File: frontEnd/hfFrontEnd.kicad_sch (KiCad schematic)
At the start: 14 parts

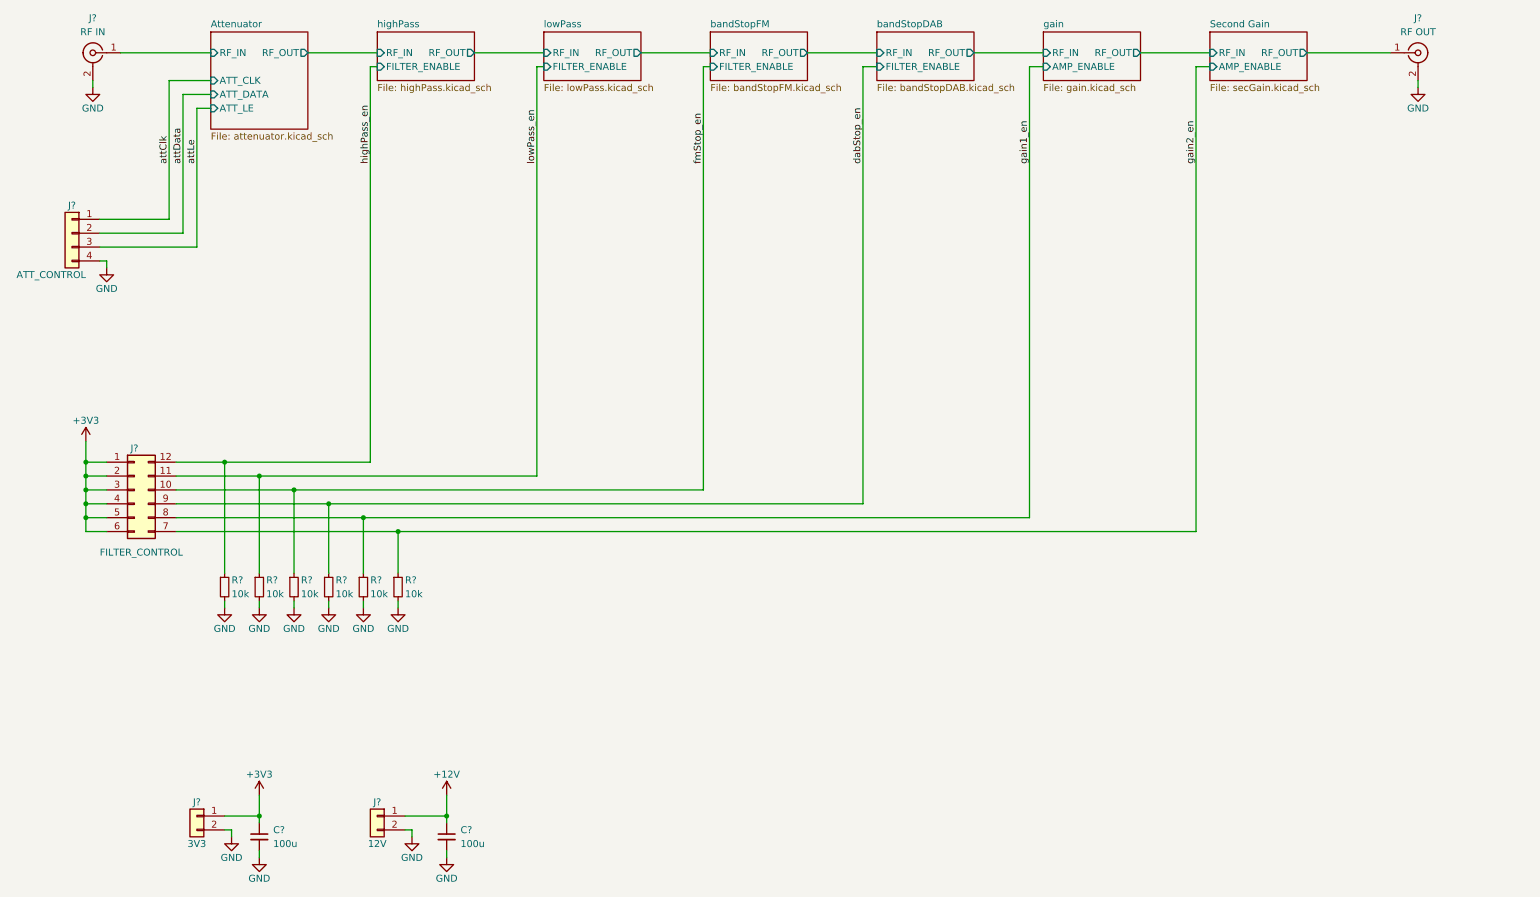
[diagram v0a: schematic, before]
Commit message: update schematics, add bypass for the attenuator
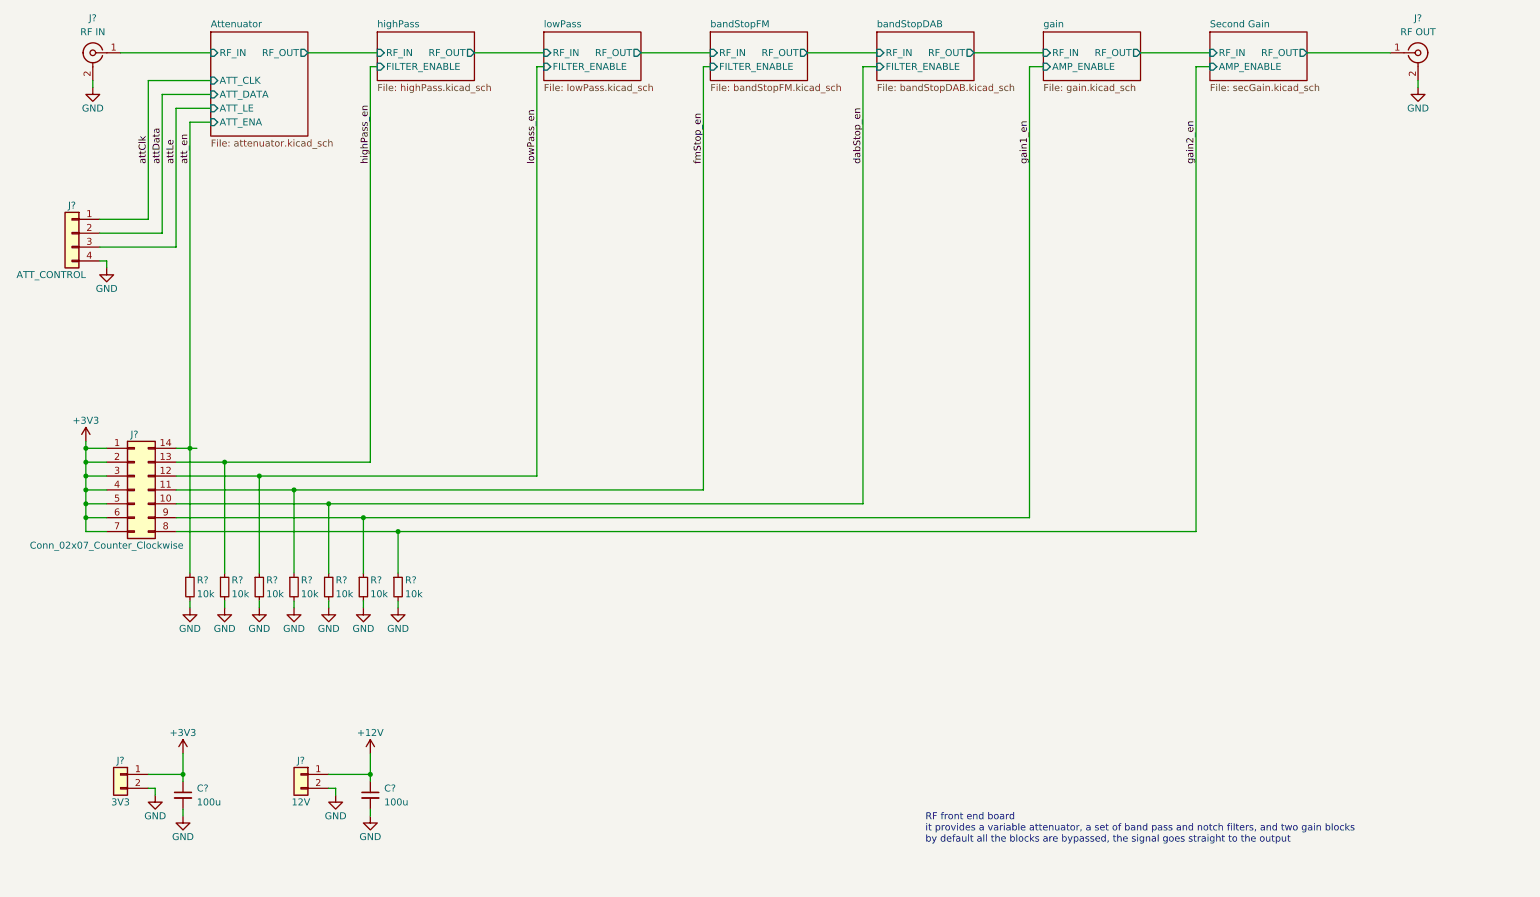
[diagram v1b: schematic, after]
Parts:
- removed J?: FILTER_CONTROL, symbol Connector_Generic:Conn_02x06_Counter_Clockwise
- added J?: Conn_02x07_Counter_Clockwise, symbol Connector_Generic:Conn_02x07_Counter_Clockwise
- added R?: 10k, symbol Device:R_Small
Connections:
- net +3V3: now also J?.1 (Pin_1), J?.2 (Pin_2), J?.3 (Pin_3), J?.4 (Pin_4), J?.5 (Pin_5), J?.6 (Pin_6), J?.7 (Pin_7)
- net GND: now also R?.2
- net dabStop_en: now also J?.10 (Pin_10)
- net fmStop_en: now also J?.11 (Pin_11)
- net gain1_en: now also J?.9 (Pin_9)
- net gain2_en: now also J?.8 (Pin_8)
- net highPass_en: now also J?.13 (Pin_13)
- net lowPass_en: now also J?.12 (Pin_12)
- new net att_en: J?.14 (Pin_14), R?.1
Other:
- sheet Attenuator ports: added ATT_ENA; removed none
- note added: "RF front end board it provides a variable attenuator, a set of band pass and notch filters, and two gain blocks by default all the blocks are bypassed, the signal goes straight to the output"
- moved on the sheet: C?, J?

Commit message: simply schematic: remove attenuator and gain blocks; add 5 way multiplexer
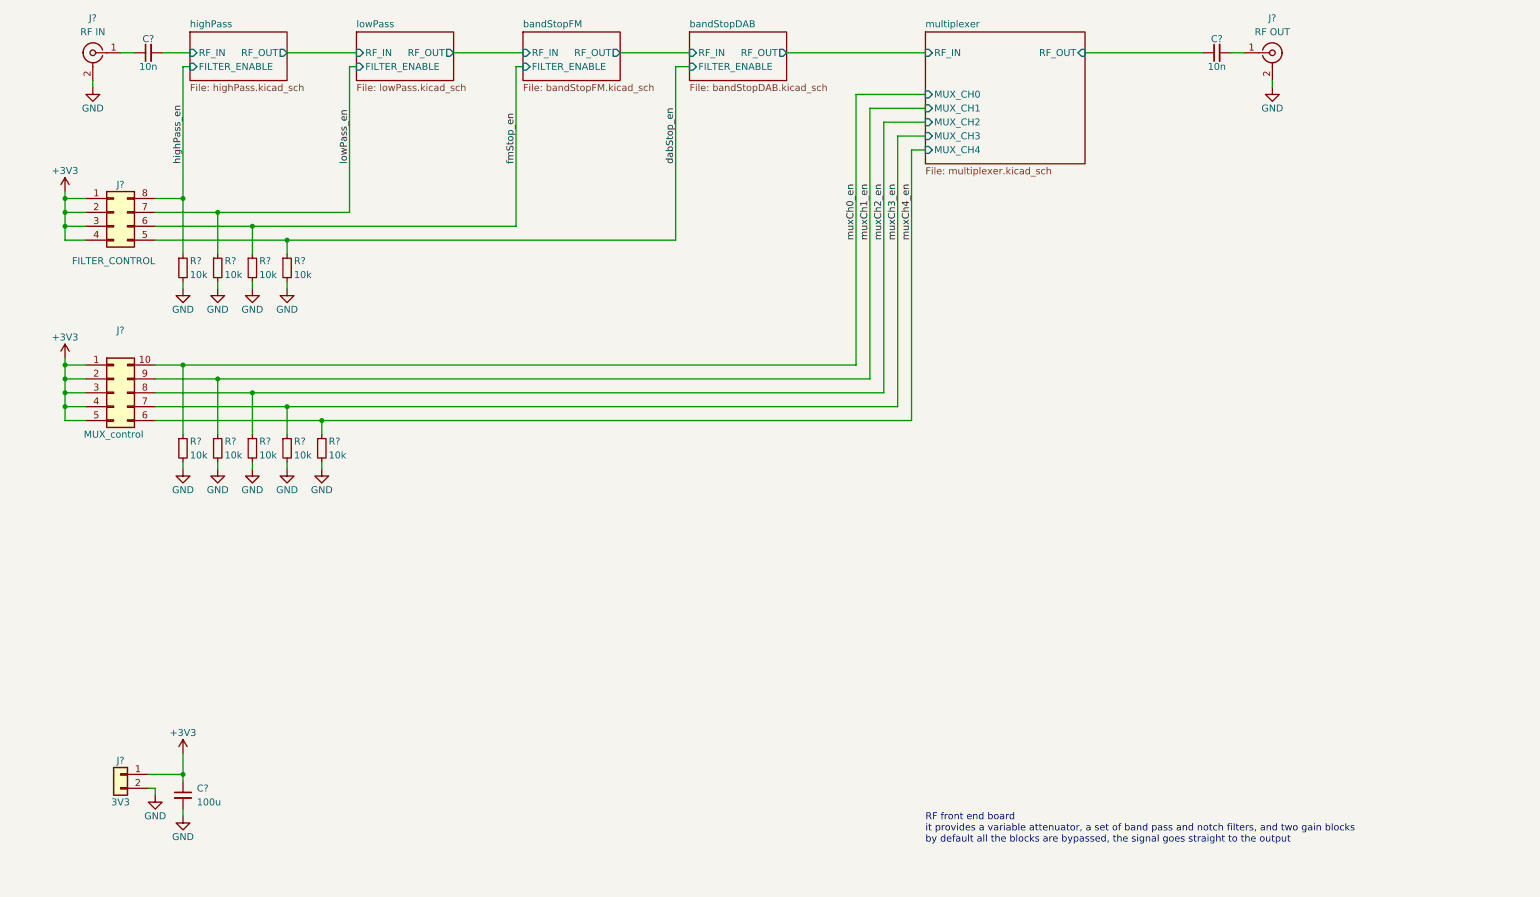
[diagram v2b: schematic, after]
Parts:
- removed C?: 100u, symbol Device:C_Small
- removed J?: Conn_02x07_Counter_Clockwise, symbol Connector_Generic:Conn_02x07_Counter_Clockwise
- removed J?: RF OUT, frontEnd:SMA, symbol Connector:Conn_Coaxial
- removed J?: ATT_CONTROL, symbol Connector_Generic:Conn_01x04
- removed J?: 12V, Connector_PinHeader_2.54mm:PinHeader_1x02_P2.54mm_Vertical, symbol Connector_Generic:Conn_01x02
- removed R? (x3): 10k, symbol Device:R_Small
- added C? (x2): 10n, Capacitor_SMD:C_0805_2012Metric, symbol Device:C_Small
- added J?: FILTER_CONTROL, symbol Connector_Generic:Conn_02x04_Counter_Clockwise
- added J?: MUX_control, symbol Connector_Generic:Conn_02x05_Counter_Clockwise
- added J?: RF OUT, frontEnd:SMA, symbol Connector:Conn_Coaxial
- added R? (x5): 10k, symbol Device:R_Small
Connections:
- net att_en is gone; now on net highPass_en: R?.1
- net +3V3: now also J?.1 (Pin_1), J?.1 (Pin_1), J?.2 (Pin_2), J?.2 (Pin_2), J?.3 (Pin_3), J?.3 (Pin_3), J?.4 (Pin_4), J?.4 (Pin_4), J?.5 (Pin_5)
- net GND: now also J?.2 (Ext), R?.2, R?.2, R?.2, R?.2, R?.2
- net dabStop_en: now also R?.1, J?.5 (Pin_5)
- net fmStop_en: now also R?.1, J?.6 (Pin_6); no longer R?.1
- net highPass_en: now also J?.8 (Pin_8); no longer R?.1
- net lowPass_en: now also R?.1, J?.7 (Pin_7); no longer R?.1
- net Attenuator/RF_IN: no longer names the net of J?.1 (In)
- net Attenuator/RF_IN: now also C?.1
- new net: C?.2, J?.1 (In)
- new net highPass/RF_IN: C?.2
- new net multiplexer/RF_OUT: C?.1
- new net muxCh0_en: J?.10 (Pin_10), R?.1
- new net muxCh1_en: J?.9 (Pin_9), R?.1
- new net muxCh2_en: J?.8 (Pin_8), R?.1
- new net muxCh3_en: J?.7 (Pin_7), R?.1
- new net muxCh4_en: J?.6 (Pin_6), R?.1
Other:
- removed sheet Attenuator
- removed sheet Second Gain
- removed sheet gain
- added sheet multiplexer (multiplexer.kicad_sch)
- moved on the sheet: R?

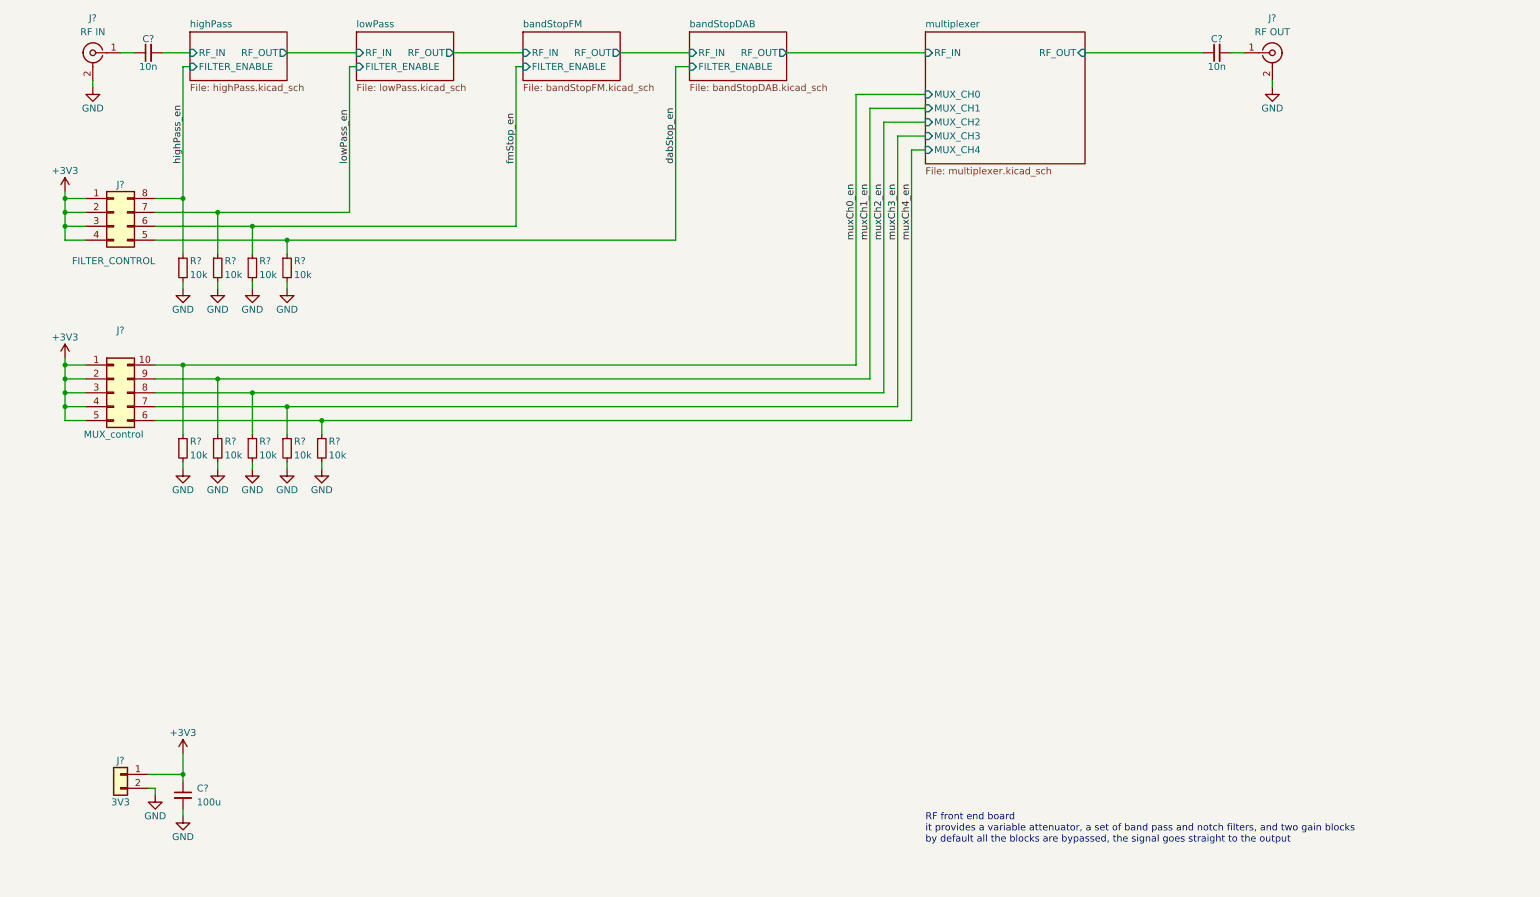
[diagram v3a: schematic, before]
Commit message: assign footprints, part designators
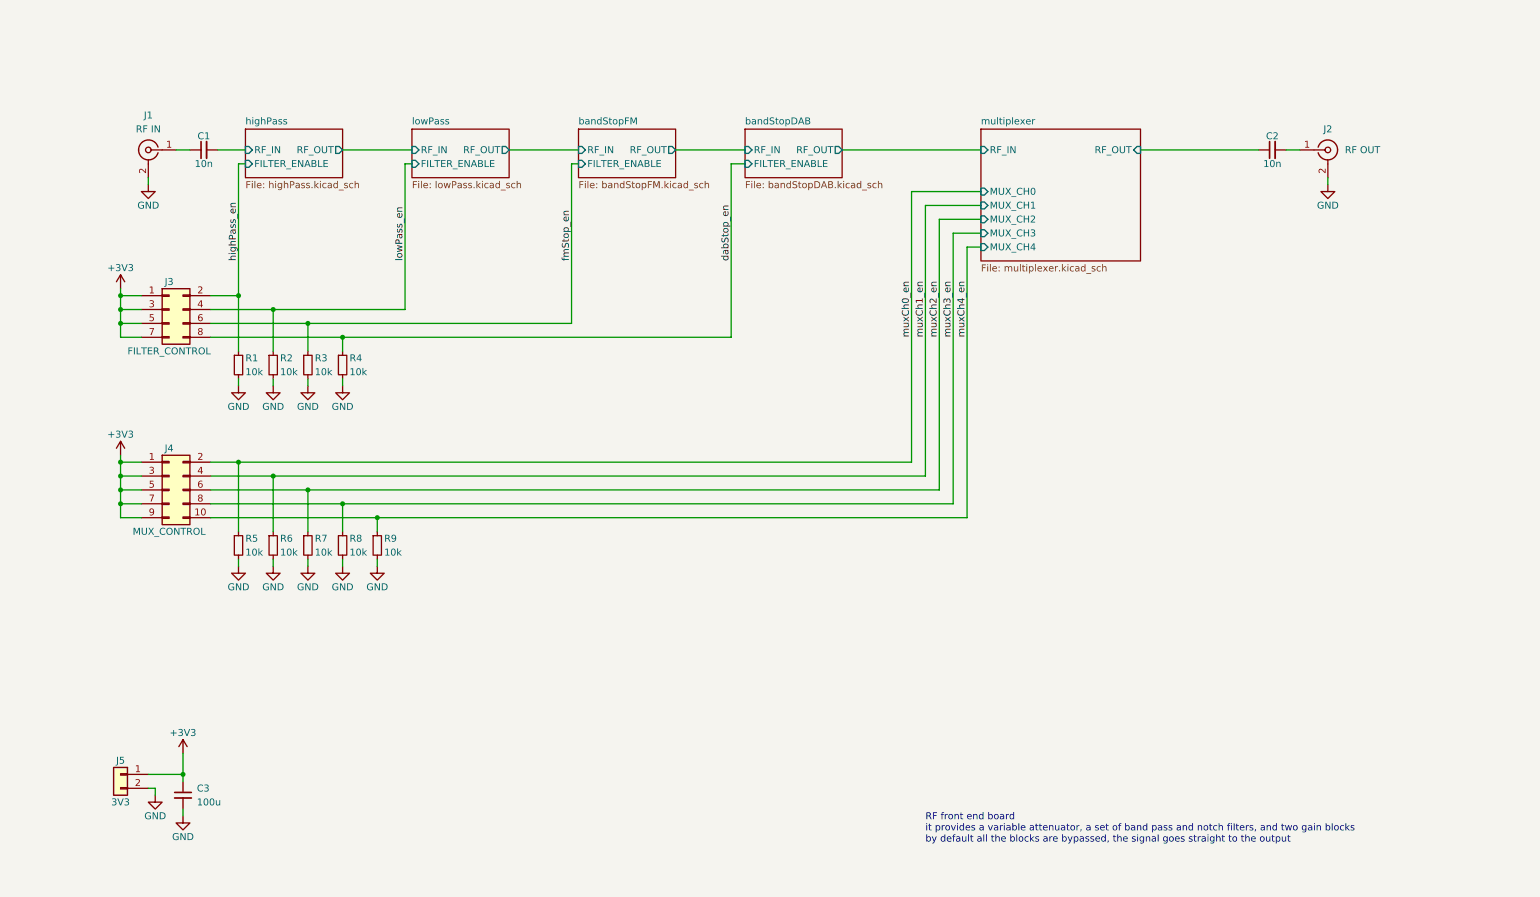
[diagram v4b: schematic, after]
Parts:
- removed J?: FILTER_CONTROL, symbol Connector_Generic:Conn_02x04_Counter_Clockwise
- removed J?: MUX_control, symbol Connector_Generic:Conn_02x05_Counter_Clockwise
- added J3: FILTER_CONTROL, Connector_PinHeader_2.54mm:PinHeader_2x04_P2.54mm_Vertical, symbol Connector_Generic:Conn_02x04_Odd_Even
- added J4: MUX_CONTROL, Connector_PinHeader_2.54mm:PinHeader_2x05_P2.54mm_Vertical, symbol Connector_Generic:Conn_02x05_Odd_Even
- C3: renamed from C?; footprint (none) -> Capacitor_THT:CP_Radial_D10.0mm_P5.00mm
- R1, R2, R3, R4, R5, R6, R7, R8, R9: renamed from R?; footprint (none) -> Resistor_SMD:R_0805_2012Metric
- gave numbers to parts that had none: 5
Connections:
- net +3V3: now also J3.1 (Pin_1), J3.3 (Pin_3), J3.5 (Pin_5), J3.7 (Pin_7), J4.1 (Pin_1), J4.3 (Pin_3), J4.5 (Pin_5), J4.7 (Pin_7), J4.9 (Pin_9)
- net dabStop_en: now also J3.8 (Pin_8)
- net fmStop_en: now also J3.6 (Pin_6)
- net highPass_en: now also J3.2 (Pin_2)
- net lowPass_en: now also J3.4 (Pin_4)
- net muxCh0_en: now also J4.2 (Pin_2)
- net muxCh1_en: now also J4.4 (Pin_4)
- net muxCh2_en: now also J4.6 (Pin_6)
- net muxCh3_en: now also J4.8 (Pin_8)
- net muxCh4_en: now also J4.10 (Pin_10)
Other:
- moved on the sheet: C1, C2, J1, J2, R1, R2, R3, R4, R5, R6, R7, R8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

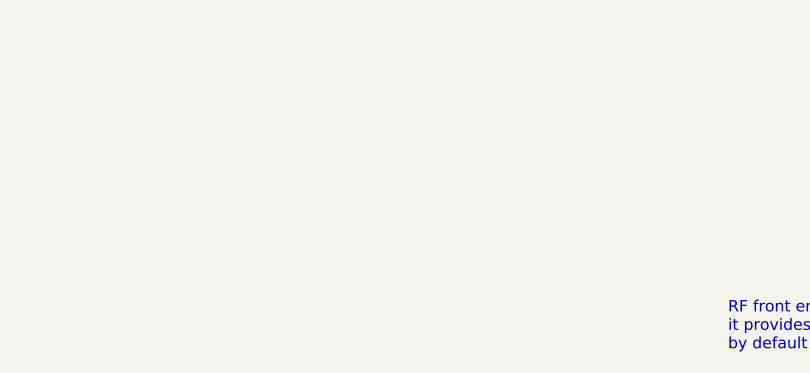
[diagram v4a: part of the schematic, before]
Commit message: convert all embeded filter to plug-in modules, start pcb layout
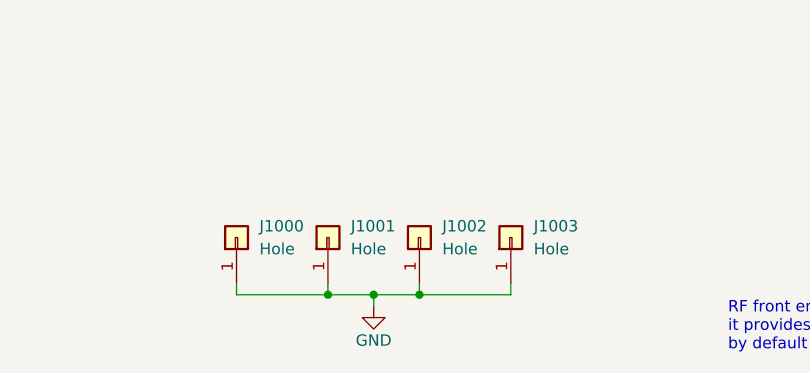
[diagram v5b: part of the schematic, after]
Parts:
- added J1000, J1001, J1002, J1003: Hole, MountingHole:MountingHole_3.2mm_M3_DIN965_Pad, symbol Connector_Generic:Conn_01x01
- C3: footprint Capacitor_THT:CP_Radial_D10.0mm_P5.00mm -> Capacitor_THT:CP_Radial_D5.0mm_P2.50mm
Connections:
- net GND: now also J1000.1 (Pin_1), J1001.1 (Pin_1), J1002.1 (Pin_1), J1003.1 (Pin_1)
